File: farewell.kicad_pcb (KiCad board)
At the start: 2 copper layers, 155.5 x 171.4 mm, 66 parts, among them J1 Conn_01x08, J2 Conn_01x08, J3 Conn_01x06, J4 Conn_01x06, SW1 SW_Push, U1 0

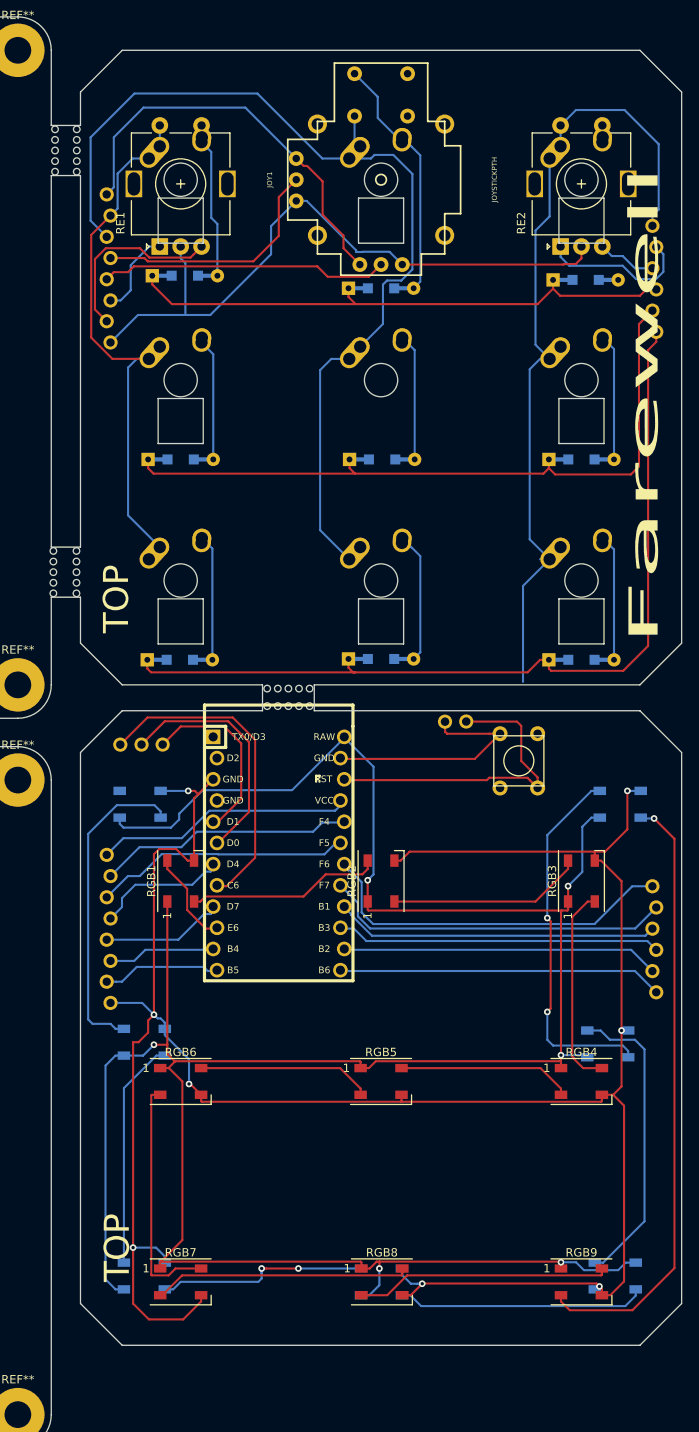
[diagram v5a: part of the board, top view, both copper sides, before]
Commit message: pcb with hybrid sk6812 mini-e/ws2812B footprint and mx/choc compatible switch footprint
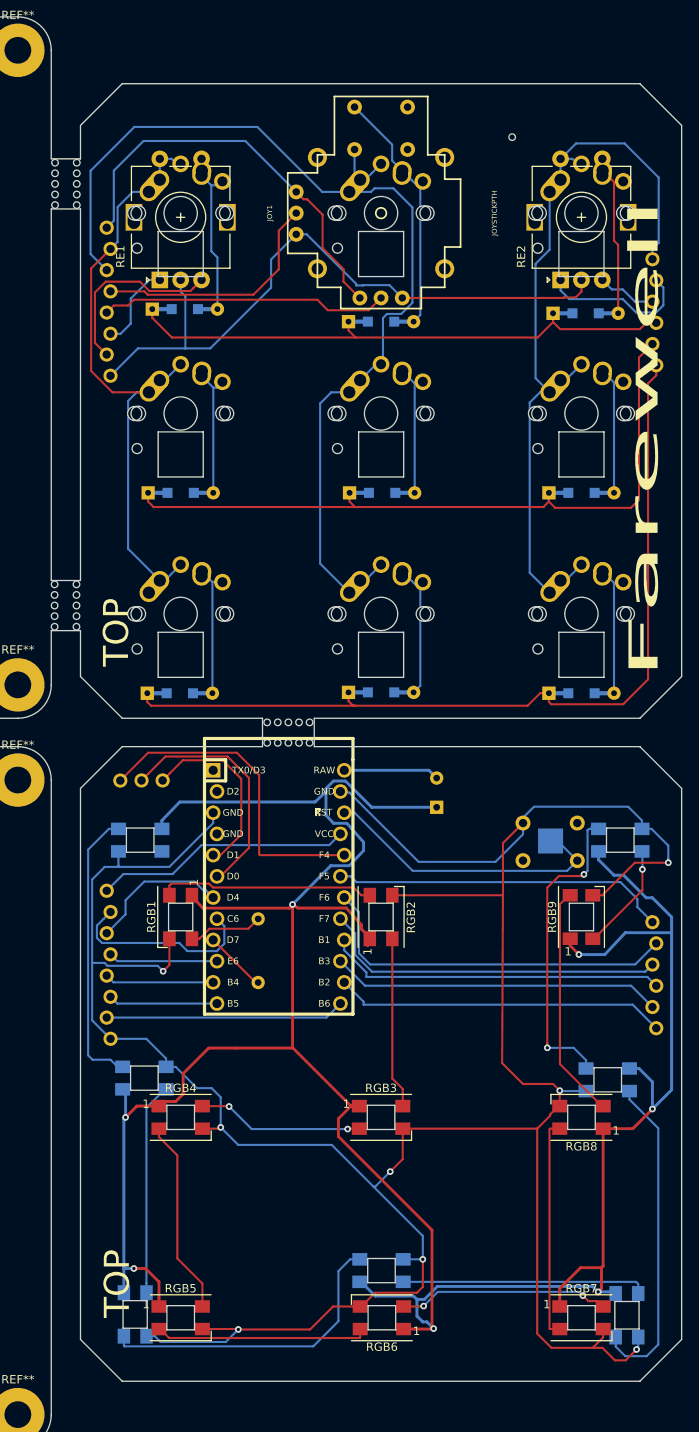
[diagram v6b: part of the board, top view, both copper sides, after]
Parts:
- removed GND_RST1, RST1: Conn_01x01, keyboard_parts:PIN_1
- added C1: 500uF, Capacitor_THT:CP_Radial_D8.0mm_P3.50mm, B.Cu at (158.3, 118.4)
- added R1: 300O, Resistor_THT:R_Axial_DIN0207_L6.3mm_D2.5mm_P7.62mm_Horizontal, B.Cu at (136.9, 139.3)
- added REF**: breakaway-hole-big, keebio:breakaway-hole-big, F.Cu at (167.3, 38.4)
- added REF**: TestPoint_Pad_3.0x3.0mm, TestPoint:TestPoint_Pad_3.0x3.0mm, B.Cu at (171.9, 122.4)
- MX1, MX2, MX3, MX4, MX5, MX6, MX7, MX8, MX9: footprint farewell:MX-1U-NoLED-NoPCBMount -> keebio:MX-Alps-Choc-1U-NoLED
- RGB1, RGB10, RGB11, RGB12, RGB13, RGB14, RGB15, RGB16, RGB2, RGB3, RGB4, RGB5, RGB6, RGB7, RGB8, RGB9: footprint LED_SMD:LED_WS2812B_PLCC4_5.0x5.0mm_P3.2mm -> farewell_pcb:LED_WS2812B_SK6812_MINI-E_HYBRID
- SW1: moved to B.Cu
- moved RGB4 48.2 mm to (127.6, 155.5)
- moved RGB7 48.2 mm to (175.6, 179.5)
- moved RGB9 43.7 mm to (175.6, 131.5), turned to 90 degrees
- moved RGB6 37.2 mm to (151.7, 179.5), turned to 180 degrees
- moved RGB5 37.1 mm to (127.6, 179.5)
- moved RGB3 37.1 mm to (151.6, 155.5), turned to 0 degrees
- moved RGB8 31.0 mm to (175.6, 155.5), turned to 180 degrees
- moved SW1 10.4 mm to (171.8, 122.5), turned to 180 degrees
- moved RGB12 4.90 mm to (181.1, 179.2), turned to 270 degrees
- moved RGB14 4.73 mm to (122.2, 179.1), turned to 270 degrees
- moved REF** 4.39 mm to (140.5, 110.9)
- moved J1 4.30 mm to (119.0, 128.4)
- moved J3 4.30 mm to (184.3, 132.1)
- moved RGB11 4.30 mm to (178.8, 151.0), turned to 180 degrees
- moved RGB15 4.30 mm to (123.2, 150.8)
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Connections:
- J1 pad 8: GND_MCU -> GND
- MX1 pad 1: COL0_SW -> Net-(D3-Pad2)
- MX1 pad 2: Net-(D3-Pad2) -> COL0_SW
- MX2 pad 1: COL1_SW -> Net-(D6-Pad2)
- MX2 pad 2: Net-(D6-Pad2) -> COL1_SW
- MX3 pad 1: COL2_SW -> Net-(D9-Pad2)
- MX3 pad 2: Net-(D9-Pad2) -> COL2_SW
- MX4 pad 1: COL0_SW -> Net-(D2-Pad2)
- MX4 pad 2: Net-(D2-Pad2) -> COL0_SW
- MX5 pad 1: COL1_SW -> Net-(D5-Pad2)
- MX5 pad 2: Net-(D5-Pad2) -> COL1_SW
- MX6 pad 1: COL2_SW -> Net-(D8-Pad2)
- MX6 pad 2: Net-(D8-Pad2) -> COL2_SW
- MX7 pad 1: COL0_SW -> RE1S1
- MX7 pad 2: RE1S1 -> COL0_SW
- MX8 pad 1: COL1_SW -> JOY_SW_1
- MX8 pad 2: JOY_SW_1 -> COL1_SW
- MX9 pad 1: COL2_SW -> RE2S1
- MX9 pad 2: RE2S1 -> COL2_SW
- RGB1 pad 3: GND_MCU -> GND
- RGB10 pad 3: GND_MCU -> GND
- RGB11 pad 3: GND_MCU -> GND
- RGB12 pad 3: GND_MCU -> GND
- RGB13 pad 3: GND_MCU -> GND
- RGB14 pad 3: GND_MCU -> GND
- RGB15 pad 3: GND_MCU -> GND
- RGB16 pad 3: GND_MCU -> GND
- RGB2 pad 3: GND_MCU -> GND
- RGB3 pad 3: GND_MCU -> GND
- RGB4 pad 3: GND_MCU -> GND
- RGB5 pad 3: GND_MCU -> GND
- RGB6 pad 3: GND_MCU -> GND
- RGB7 pad 3: GND_MCU -> GND
- RGB8 pad 3: GND_MCU -> GND
- RGB9 pad 3: GND_MCU -> GND
- SW1 pad 1: Net-(GND_RST1-Pad1) -> GND
- U1 pad 10: RGB_DI -> ADC1_MCU
- U1 pad 11: E1A_MCU -> ADC2_MCU
- U1 pad 12: E1B_MCU -> E1A_MCU
- U1 pad 13: ROW0_MCU -> E1B_MCU
- U1 pad 14: ROW1_MCU -> ROW0_MCU
- U1 pad 15: ROW2_MCU -> ROW1_MCU
- U1 pad 16: E2B_MCU -> ROW2_MCU
- U1 pad 17: E2A_MCU -> E2B_MCU
- U1 pad 18: COL2_MCU -> E2A_MCU
- U1 pad 19: COL1_MCU -> COL2_MCU
- U1 pad 20: COL0_MCU -> Net-(EXT1-Pad1)
- U1 pad 23: Net-(GND_RST1-Pad1) -> GND
- U1 pad 24: RGB_VCC -> Net-(C1-Pad2)
- U1 pad 3: GND_MCU -> GND
- U1 pad 7: ADC1_MCU -> COL1_MCU
- U1 pad 8: Net-(EXT1-Pad1) -> COL0_MCU
- U1 pad 9: ADC2_MCU -> Net-(R1-Pad1)
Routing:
- net GND: track 0.00 -> 345.8 mm, vias 0 -> 8
- net GND_MCU: track 284.8 -> 0.00 mm, vias 8 -> 0
- net Net-(RGB10-Pad4): track 72.7 -> 13.9 mm
- net Net-(GND_RST1-Pad1): track 27.9 -> 0.00 mm
- net RGB_VCC: track 310.5 -> 335.6 mm, vias 6 -> 7
- net RE2S1: track 2.00 -> 19.9 mm
- net E1B_MCU: track 14.2 -> 28.7 mm
- net COL1_MCU: track 31.2 -> 17.1 mm
- net Net-(RGB13-Pad2): track 25.5 -> 37.4 mm, vias 2 -> 0
- net Net-(C1-Pad2): track 0.00 -> 11.6 mm
- net COL0_SW: track 64.1 -> 73.4 mm
- net Net-(R1-Pad1): track 0.00 -> 7.50 mm
- net COL0_MCU: track 30.7 -> 23.4 mm
- net COL1_SW: track 116.3 -> 122.8 mm
- net Net-(RGB10-Pad2): track 44.3 -> 38.3 mm
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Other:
- outline, holes or cut-outs redrawn
- net class RGB_VCC added: clearance 0.2, trace_width 0.35, via_dia 0.8, via_drill 0.4
- board text added: "C6"
- board text removed: "ADC1"
- board text removed: "ADC2"
- board text removed: "EXT. C6"
- board text removed: "Gnd"
- board text removed: "Reset"

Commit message: Complete pcb
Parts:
- removed EXT1: Conn_01x01, keyboard_parts:PIN_1
- removed J1, J2: Conn_01x08, farewell_pcb:keebio_Header-8-Pin-ZigZag
- removed J3, J4: Conn_01x06, farewell_pcb:keebio_Header-6-Pin-ZigZag
- removed the REF** at (167.3, 38.4)
- removed the REF** at (96.1, 110.3)
- removed the REF** at (45.5, 110.3)
- removed the REF** at (45.5, 108.5)
- removed the REF** at (96.1, 108.5)
- removed the REF** at (140.5, 108.4)
- removed the REF** at (140.5, 110.9)
- removed SW1: SW_Push, random-kb-part:PushButton_6x6mm_TH_Pretty
- added REF**: breakaway-mousebites, random-kb-part:breakaway-mousebites, F.Cu at (190.5, 43.7)
- added REF**: breakaway-mousebites, random-kb-part:breakaway-mousebites, F.Cu at (190.5, 94.2)
- added REF**: breakaway-mousebites, random-kb-part:breakaway-mousebites, F.Cu at (187.8, 94.2)
- added REF**: breakaway-mousebites, random-kb-part:breakaway-mousebites, F.Cu at (187.8, 43.7)
- MX1, MX2, MX3, MX4, MX5, MX6, MX7, MX8, MX9: footprint keebio:MX-Alps-Choc-1U-NoLED -> farewell_pcb:MX-Alps-Choc-1U-NoLED-noprongs
- RE1, RE2: footprint Encoders:RotaryEncoder_Alps_EC11E-Switch_Vertical_H20mm -> farewell_pcb:RotaryEncoder_Alps_EC11E-Switch_Vertical_H20mm_noleg
- RGB1, RGB3, RGB5, RGB6, RGB8: footprint farewell_pcb:LED_WS2812B_SK6812_MINI-E_HYBRID -> farewell_pcb:SK6812_MINI-E_FACEDOWN; moved to B.Cu
- RGB10, RGB13, RGB15, RGB16: footprint farewell_pcb:LED_WS2812B_SK6812_MINI-E_HYBRID -> farewell_pcb:SK6812_MINI-E_FACEDOWN
- RGB2, RGB4, RGB7, RGB9: moved to B.Cu
- U1: footprint farewell_pcb:keebio_ArduinoProMicro-ZigZag -> farewell_pcb:keebio_ArduinoProMicro-ZigZag-noF4
- moved REF** 181.4 mm to (267.1, 103.7)
- moved REF** 181.4 mm to (267.1, 27.7)
- moved REF** 181.4 mm to (195.1, 103.7)
- moved REF** 181.4 mm to (195.1, 27.7)
- moved RGB14 126.6 mm to (121.7, 52.5)
- moved RGB12 118.4 mm to (122.0, 76.6)
- moved RGB5 105.5 mm to (151.6, 76.8), turned to 180 degrees
- moved RGB13 100.0 mm to (127.6, 76.7)
- moved RGB15 98.4 mm to (127.5, 52.5)
- moved RGB4 95.6 mm to (181.1, 76.2), turned to 270 degrees
- moved RGB1 91.7 mm to (175.1, 53.0), turned to 0 degrees
- moved C1 88.6 mm to (131.4, 34.0), turned to 270 degrees
- moved U1 87.4 mm to (172.8, 47.1)
- moved R1 85.5 mm to (168.7, 60.0)
- moved REF** 85.0 mm to (184.4, 38.3)
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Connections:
- C1 pad 2: Net-(C1-Pad2) -> GND
- JOY1 pad H1: VCC_SW -> VCC
- JOY1 pad H3: GND_SW -> GND
- JOY1 pad V1: VCC_SW -> VCC
- JOY1 pad V3: GND_SW -> GND
- RE1 pad C: GND_SW -> GND
- RE2 pad C: GND_SW -> GND
- REF** pad 1: Net-(SW1-Pad2) -> GND
- U1 pad 10: ADC1_MCU -> ADC1_SW
- U1 pad 11: ADC2_MCU -> ADC2_SW
- U1 pad 12: E1A_MCU -> E1A_SW
- U1 pad 13: E1B_MCU -> E1B_SW
- U1 pad 14: ROW0_MCU -> ROW0_SW
- U1 pad 15: ROW1_MCU -> ROW1_SW
- U1 pad 16: ROW2_MCU -> ROW2_SW
- U1 pad 17: E2B_MCU -> E2B_SW
- U1 pad 18: E2A_MCU -> E2A_SW
- U1 pad 19: COL2_MCU -> COL2_SW
- U1 pad 21: VCC_MCU -> VCC
- U1 pad 22: Net-(SW1-Pad2) -> Net-(U1-Pad22)
- U1 pad 24: Net-(C1-Pad2) -> RGB_VCC
- U1 pad 7: COL1_MCU -> COL1_SW
- U1 pad 8: COL0_MCU -> COL0_SW
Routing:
- net (no net): track 0.00 -> 206.5 mm
- net RGB_VCC: track 335.6 -> 418.9 mm, vias 7 -> 6
- net GND_SW: track 78.8 -> 0.00 mm
- net VCC: track 0.00 -> 74.6 mm
- net GND: track 345.8 -> 403.3 mm, vias 8 -> 15
- net COL0_SW: track 73.4 -> 126.0 mm, vias 0 -> 1
- net VCC_SW: track 49.1 -> 0.00 mm
- net E2A_MCU: track 44.6 -> 0.00 mm
- net E2B_MCU: track 41.8 -> 0.00 mm
- net COL2_MCU: track 41.3 -> 0.00 mm
- net ROW2_MCU: track 40.7 -> 0.00 mm
- net ROW0_MCU: track 39.9 -> 0.00 mm
- net ROW1_MCU: track 39.7 -> 0.00 mm
- net Net-(EXT1-Pad1): track 38.8 -> 0.00 mm
- net Net-(SW1-Pad2): track 36.6 -> 0.00 mm
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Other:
- board size 155.5 x 171.4 mm -> 239 x 84 mm
- net class Net-(C1-Pad2) added: clearance 0.2, trace_width 0.35, via_dia 0.8, via_drill 0.4
- board text added: "."
- board text removed: "C6"
- board text removed: "Vcc"
